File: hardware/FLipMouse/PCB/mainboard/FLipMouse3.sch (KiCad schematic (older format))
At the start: 81 parts, among them J1 SJ2-3574A, J2 SJ2-3574A, J3 M50-3900542, J4 Conn_ARM_JTAG_SWD_10, J5 Conn_02x05_Odd_Even, J6 USB_OTG, J7 Conn_01x06, Q1 BC847, Q2 BC847, Q3 BSH108, Q4 BSH108, Q5 BSH108, SW1 SW_Push, SW2 SW_Push, U1 ESP32-WROOM, U2 TSOP4838, U3 LPC11U14FBD, U4 TSR_1-2433, U5 MPXV7007GP, Y1 JA-12.000-18-DFE

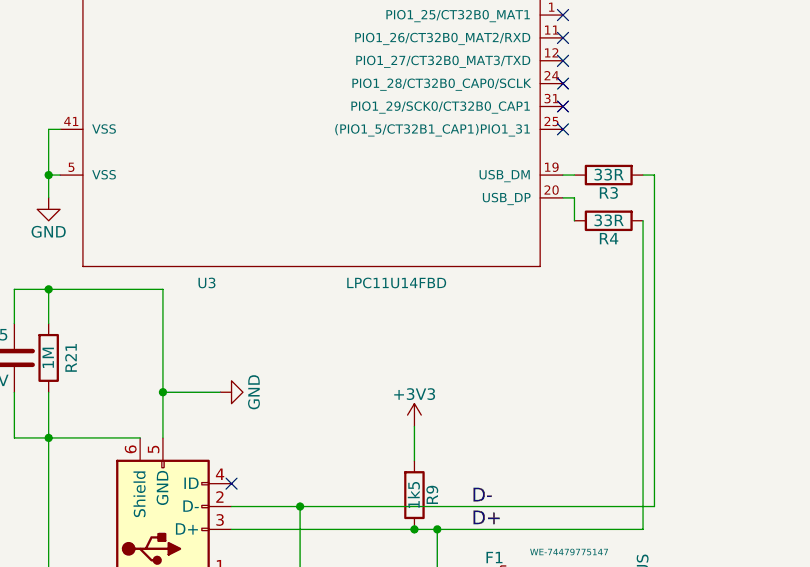
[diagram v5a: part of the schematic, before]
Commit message: Changed USB chipset to LPC11U__2__4 (from LPC11U14): This introduces the possibility to use the USB-MSD bootloader for software updates. Otherwise we would need either a serial adapter, a custom bootloader or a programming software within the ESP32 (and more nets between these two chips).
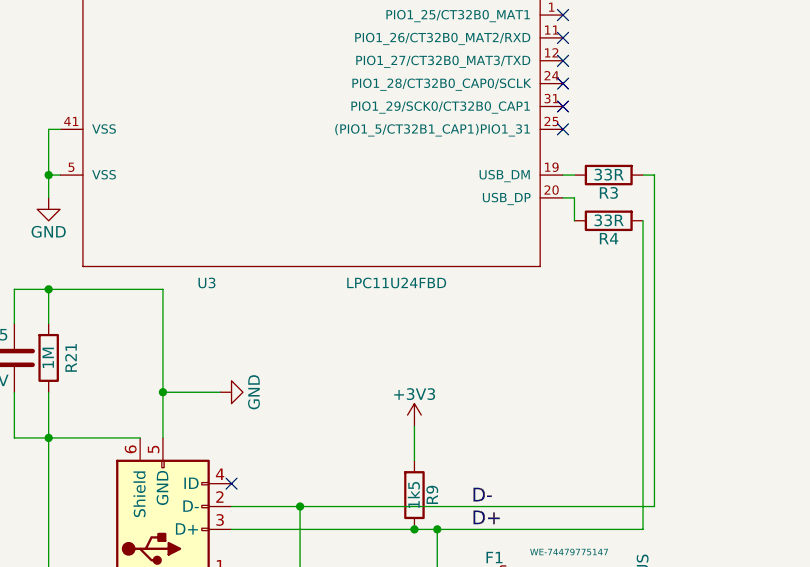
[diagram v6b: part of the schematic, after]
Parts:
- U3: value LPC11U14FBD -> LPC11U24FBD
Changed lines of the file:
@@
 P 2400 3500
 F 0 "U3" H 1900 1000 45  0000 L BNN
-F 1 "LPC11U14FBD" H 2550 1000 45  0000 L BNN
+F 1 "LPC11U24FBD" H 2550 1000 45  0000 L BNN
 F 2 "Package_QFP:LQFP-48_7x7mm_P0.5mm" H 2430 3650 20  0001 C CNN
 F 3 "" H 2400 3500 60  0001 C CNN

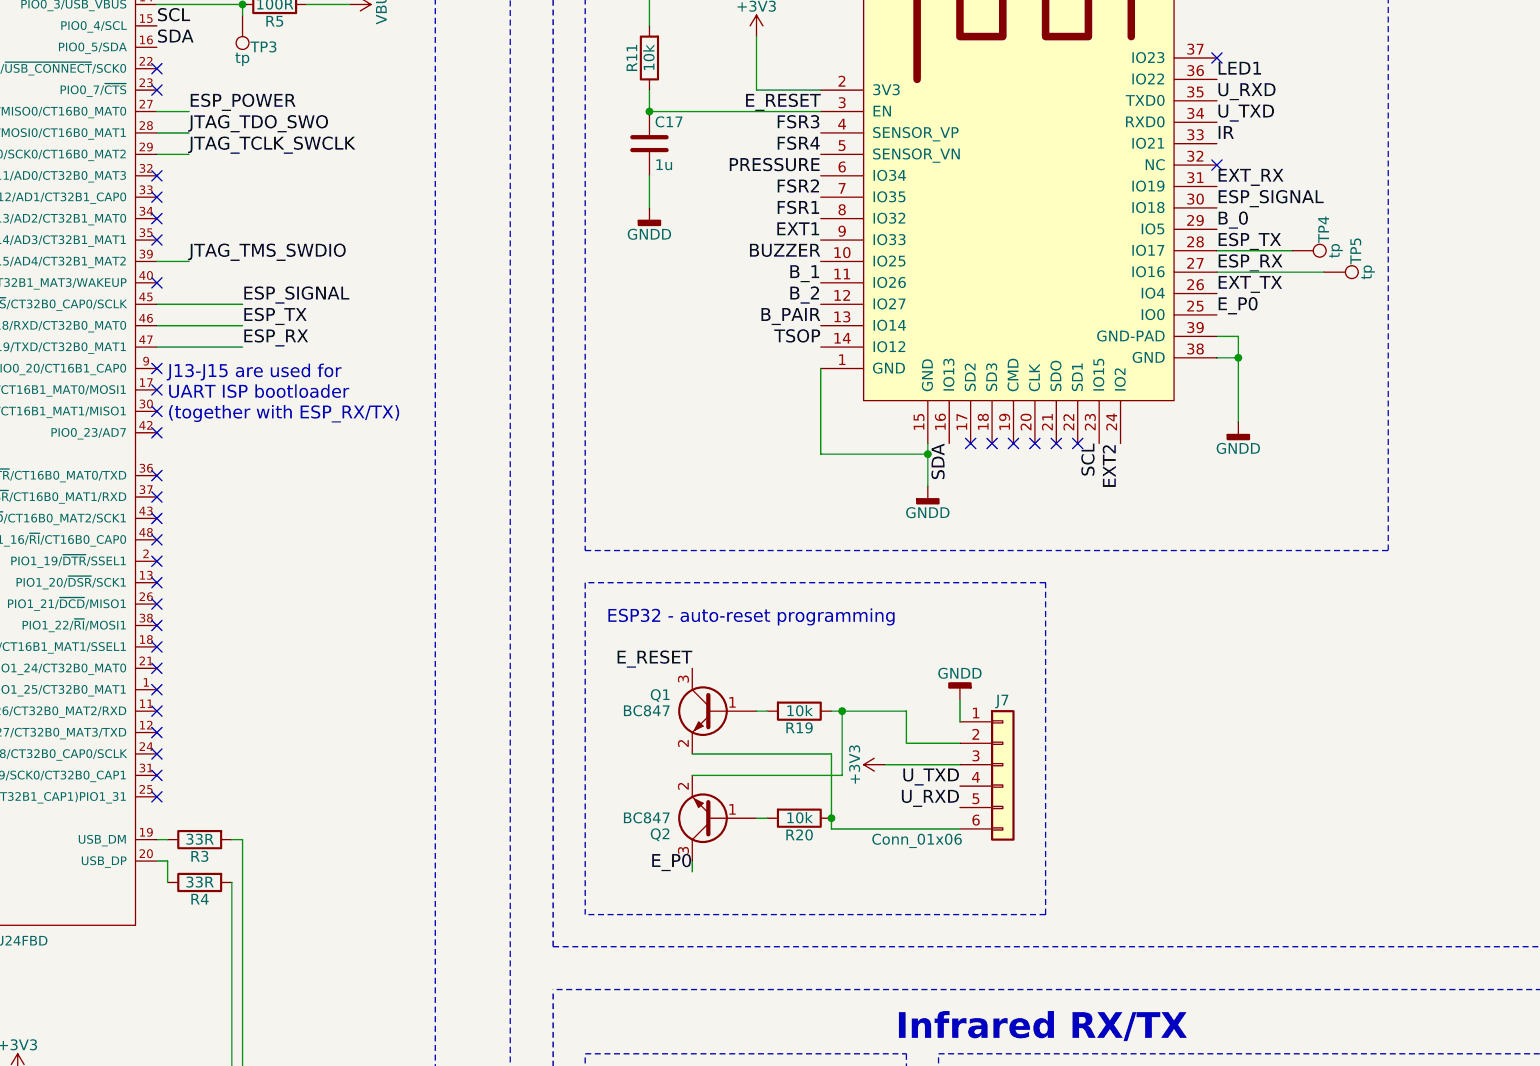
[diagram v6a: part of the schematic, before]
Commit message: Updated FLipMouse PCB: - Routed ADC inputs (FSR+pressure) to LPC11 too (in case of crappy ESP ADC values) - Added ESP32 auto-reset pins to LPC11 (enabling programming via LPC USB) - Cleanup regarding edge to trace spacing
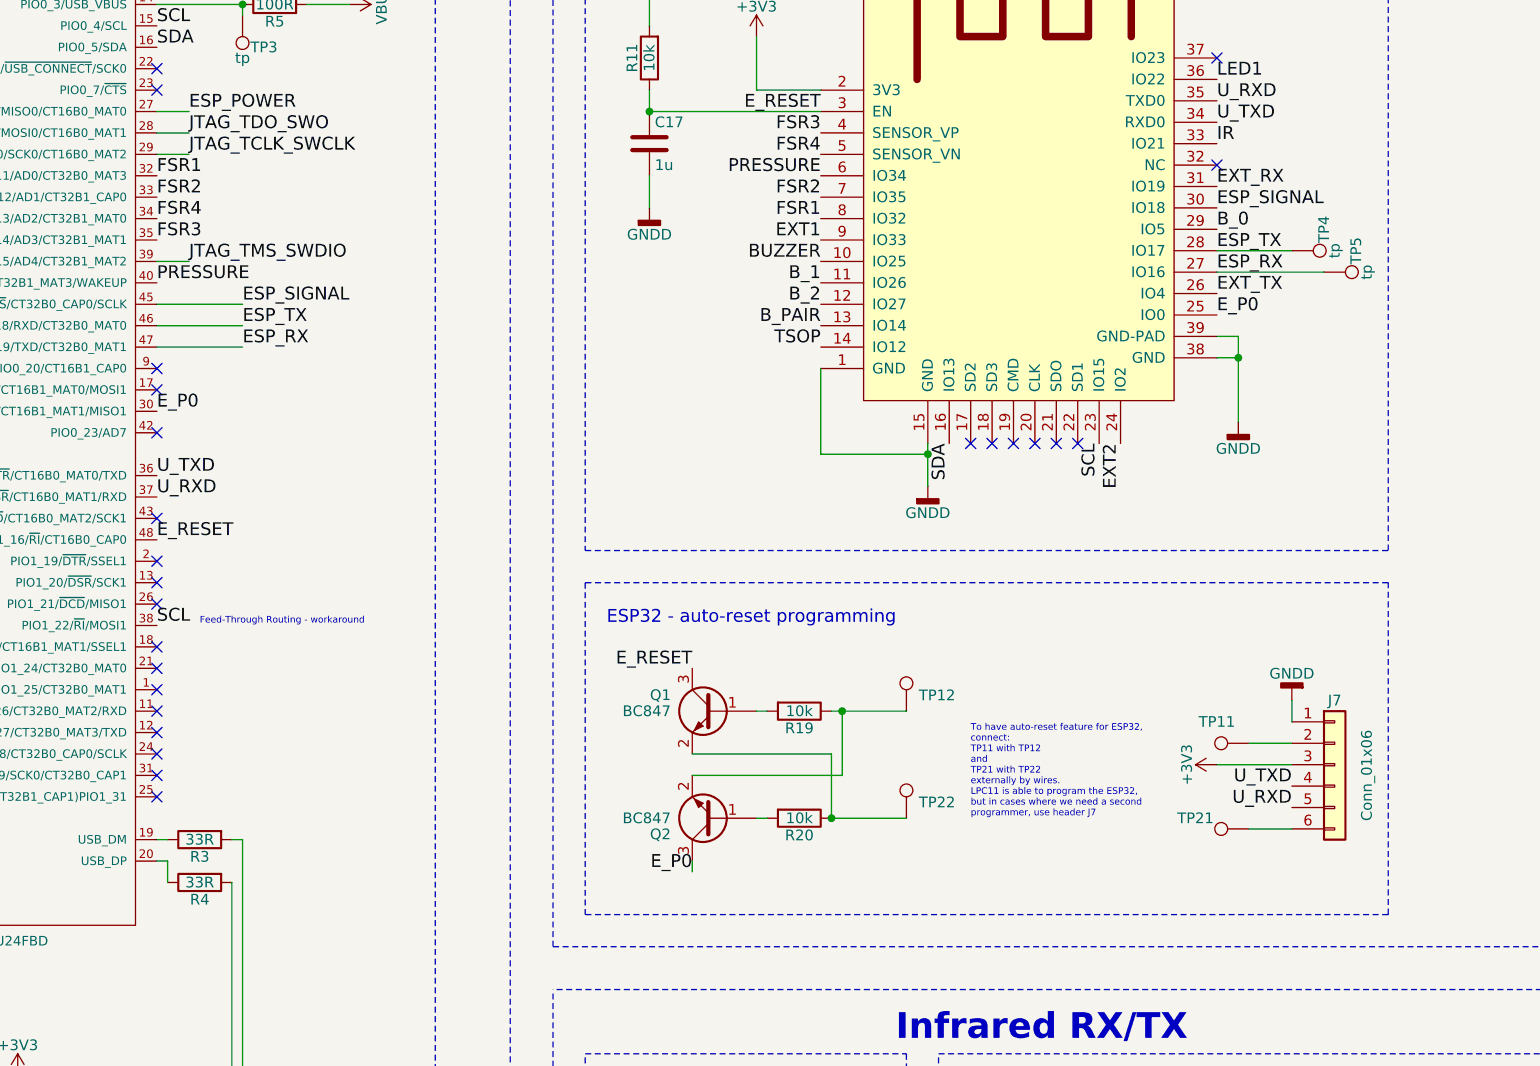
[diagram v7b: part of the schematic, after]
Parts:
- added TP11, TP12, TP21, TP22: TP, TestPoint:TestPoint_Pad_D1.0mm, symbol Connector:TestPoint
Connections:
- net E_P0: now also U3.30 (PIO0_22/AD6/CT16B1_MAT1/MISO1)
- net E_RESET: now also U3.48 (PIO1_16/~RI~/CT16B0_CAP0)
- net FSR1: now also U3.32 (TDI/PIO0_11/AD0/CT32B0_MAT3)
- net FSR2: now also U3.33 (TMS/PIO0_12/AD1/CT32B1_CAP0)
- net FSR3: now also U3.35 (~TRST~/PIO0_14/AD3/CT32B1_MAT1)
- net FSR4: now also U3.34 (TDO/PIO0_13/AD2/CT32B1_MAT0)
- net PRESSURE: now also U3.40 (PIO0_16/AD5/CT32B1_MAT3/WAKEUP)
- net SCL: now also U3.38 (PIO1_22/~RI~/MOSI1)
- net U_RXD: now also U3.37 (PIO1_14/~DSR~/CT16B0_MAT1/RXD)
- net U_TXD: now also U3.36 (PIO1_13/~DTR~/CT16B0_MAT0/TXD)
- net at Q2.2 (E), R19.1: now also TP12.1; no longer J7.2 (Pin_2)
- net at Q1.2 (E), R20.1: now also TP22.1; no longer J7.6 (Pin_6)
- new net: J7.2 (Pin_2), TP11.1
- new net: J7.6 (Pin_6), TP21.1
- no-connect marks 45 -> 35
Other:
- note added: "Feed-Through Routing - workaround"
- note added: "To have auto-reset feature for ESP32,\nconnect:\nTP11 with TP12\nand\nTP21 with TP22\nexternally by wires.\nLPC11 is able to program the ESP32, \nbut in cases where we need a second \nprogrammer, use header J7"
- note removed: "J13-J15 are used for \nUART ISP bootloader\n(together with ESP_RX/TX)"
- moved on the sheet: J7
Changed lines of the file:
@@
 Sheet 1 1
 Title "FLipMouse3"
-Date "2018-11-15"
+Date "2018-12-02"
 Rev "v3.1"
 Comp "AsTeRICS Foundation"
@@
 L Connector_Generic:Conn_01x06 J7
 U 1 1 5A82E80B
-P 7450 5150
-F 0 "J7" H 7450 5450 50  0000 C CNN
-F 1 "Conn_01x06" H 7050 4800 50  0000 C CNN
-F 2 "Connector_PinSocket_1.27mm:PinSocket_1x06_P1.27mm_Vertical" H 7450 5150 50  0001 C CNN
-F 3 "" H 7450 5150 50  0001 C CNN
-	1    7450 5150
+P 9000 5150
+F 0 "J7" H 9000 5450 50  0000 C CNN
+F 1 "Conn_01x06" V 9150 5100 50  0000 C CNN
+F 2 "Connector_PinSocket_1.27mm:PinSocket_1x06_P1.27mm_Vertical" H 9000 5150 50  0001 C CNN
+F 3 "" H 9000 5150 50  0001 C CNN
+	1    9000 5150
 	1    0    0    -1
 $EndComp
@@
 	0    1    1    0
 $EndComp
-Text Label 7250 5350 2    60   ~ 0
+Text Label 8800 5350 2    60   ~ 0
 U_RXD
-Text Label 7250 5250 2    60   ~ 0
+Text Label 8800 5250 2    60   ~ 0
 U_TXD
 $Comp
 L power:GNDD #PWR020
 U 1 1 5A83058B
-P 7250 4850
-F 0 "#PWR020" H 7250 4600 50  0001 C CNN
-F 1 "GNDD" H 7250 4725 50  0000 C CNN
-F 2 "" H 7250 4850 50  0001 C CNN
-F 3 "" H 7250 4850 50  0001 C CNN
-	1    7250 4850
+P 8800 4850
+F 0 "#PWR020" H 8800 4600 50  0001 C CNN
+F 1 "GNDD" H 8800 4725 50  0000 C CNN
+F 2 "" H 8800 4850 50  0001 C CNN
+F 3 "" H 8800 4850 50  0001 C CNN
+	1    8800 4850
 	-1   0    0    1
 $EndComp
@@
 L power:+3V3 #PWR021
 U 1 1 5A83079E
-P 6900 5150
-F 0 "#PWR021" H 6900 5000 50  0001 C CNN
-F 1 "+3V3" H 6900 5290 50  0000 C CNN
-F 2 "" H 6900 5150 50  0001 C CNN
-F 3 "" H 6900 5150 50  0001 C CNN
-	1    6900 5150
+P 8450 5150
+F 0 "#PWR021" H 8450 5000 50  0001 C CNN
+F 1 "+3V3" H 8450 5290 50  0000 C CNN
+F 2 "" H 8450 5150 50  0001 C CNN
+F 3 "" H 8450 5150 50  0001 C CNN
+	1    8450 5150
 	0    -1   -1   0
 $EndComp
@@
 NoConn ~ 3500 1500
 NoConn ~ 3500 2000
-NoConn ~ 3500 4100
-NoConn ~ 3500 2400
-NoConn ~ 3500 2600
-NoConn ~ 3500 2500
-NoConn ~ 3500 2700
-NoConn ~ 3500 2900
+NoConn ~ 3500 5200
 NoConn ~ 3500 3300
 NoConn ~ 3500 3600
-NoConn ~ 3500 3800
 NoConn ~ 3500 4300
 NoConn ~ 3500 4400
-NoConn ~ 3500 4500
 NoConn ~ 3500 4600
 NoConn ~ 3500 4800
 NoConn ~ 3500 5100
-NoConn ~ 3500 5200
 NoConn ~ 3500 5300
 NoConn ~ 8450 2350
@@
 NoConn ~ 3500 5000
 NoConn ~ 3500 4900
-NoConn ~ 3500 3900
 Text Label 7200 3650 3    60   ~ 0
 SDA
@@
 Wire Wire Line
 	6000 5200 6700 5200
-Connection ~ 6650 5400
 Wire Wire Line
 	6000 5100 6650 5100
 Wire Wire Line
-	6650 5450 7250 5450
-Wire Wire Line
 	6650 5100 6650 5400
 Wire Wire Line
@@
 	6650 4900 6700 4900
 Wire Wire Line
-	7000 4900 7000 5050
-Wire Wire Line
-	7000 5050 7250 5050
-Wire Wire Line
-	6900 5150 7250 5150
-Wire Wire Line
-	7250 4950 7250 4850
+	8450 5150 8800 5150
+Wire Wire Line
+	8800 4950 8800 4850
 Connection ~ 15100 5500
 Wire Wire Line
@@
 	14750 2250 14750 900
 Wire Notes Line
-	7650 5850 7650 4300
-Wire Notes Line
-	7650 4300 5500 4300
+	9250 5850 9250 4300
+Wire Notes Line
+	9250 4300 5500 4300
 Wire Notes Line
 	5500 4300 5500 5850
@@
 Wire Wire Line
 	6700 4900 7000 4900
-Wire Wire Line
-	6650 5400 6650 5450
 Wire Wire Line
 	15100 5500 15350 5500
@@
 SCL
 NoConn ~ 3500 3400
-NoConn ~ 3500 3500
 NoConn ~ 3500 4000
 NoConn ~ 3500 4200
@@
 Wire Wire Line
 	3500 1600 3900 1600
-Text Notes 3550 3550 0    60   ~ 0
-J13-J15 are used for \nUART ISP bootloader\n(together with ESP_RX/TX)
 Text Notes 12350 800  0    120  ~ 24
 User Input / Output
@@
 Extension header
 Wire Notes Line
-	7650 5850 5500 5850
+	9250 5850 5500 5850
 Text Notes 6550 800  0    120  ~ 24
 ESP32 - main processor
@@
 	11500 1700 11500 2300
 NoConn ~ 11400 2000
+Text Label 3500 2400 0    60   ~ 0
+FSR1
+Text Label 3500 2500 0    60   ~ 0
+FSR2
+Text Label 3500 2700 0    60   ~ 0
+FSR3
+Text Label 3500 2600 0    60   ~ 0
+FSR4
+Text Label 3500 2900 0    60   ~ 0
+PRESSURE
+Text Label 3500 3500 0    60   ~ 0
+E_P0
+Text Label 3500 3800 0    60   ~ 0
+U_TXD
+Text Label 3500 3900 0    60   ~ 0
+U_RXD
+Text Label 3500 4100 0    60   ~ 0
+E_RESET
+$Comp
+L Connector:TestPoint TP11
+U 1 1 5C06E7F7
+P 8600 5050
+F 0 "TP11" V 8700 5200 50  0000 C CNN
+F 1 "TP" V 8704 5124 50  0001 C CNN
+F 2 "TestPoint:TestPoint_Pad_D1.0mm" H 8800 5050 50  0001 C CNN
+F 3 "~" H 8800 5050 50  0001 C CNN
+	1    8600 5050
+	0    -1   -1   0
+$EndComp
+$Comp
+L Connector:TestPoint TP21
+U 1 1 5C06E8C9
+P 8600 5450
+F 0 "TP21" V 8650 5700 50  0000 C CNN
+F 1 "TP" V 8700 5650 50  0001 C CNN
+F 2 "TestPoint:TestPoint_Pad_D1.0mm" H 8800 5450 50  0001 C CNN
+F 3 "~" H 8800 5450 50  0001 C CNN
+	1    8600 5450
+	0    -1   -1   0
+$EndComp
+$Comp
+L Connector:TestPoint TP12
+U 1 1 5C06E995
+P 7000 4900
+F 0 "TP12" H 7058 4974 50  0000 L CNN
+F 1 "TP" H 7058 4929 50  0001 L CNN
+F 2 "TestPoint:TestPoint_Pad_D1.0mm" H 7200 4900 50  0001 C CNN
+F 3 "~" H 7200 4900 50  0001 C CNN
+	1    7000 4900
+	1    0    0    -1
+$EndComp
+$Comp
+L Connector:TestPoint TP22
+U 1 1 5C06EA65
+P 7000 5400
+F 0 "TP22" H 7058 5474 50  0000 L CNN
+F 1 "TP" H 7058 5429 50  0001 L CNN
+F 2 "TestPoint:TestPoint_Pad_D1.0mm" H 7200 5400 50  0001 C CNN
+F 3 "~" H 7200 5400 50  0001 C CNN
+	1    7000 5400
+	1    0    0    -1
+$EndComp
+Wire Wire Line
+	6650 5400 7000 5400
+Connection ~ 6650 5400
+Wire Wire Line
+	8600 5050 8800 5050
+Wire Wire Line
+	8600 5450 8800 5450
+Text Notes 7300 5400 0    31   ~ 0
+To have auto-reset feature for ESP32,\nconnect:\nTP11 with TP12\nand\nTP21 with TP22\nexternally by wires.\nLPC11 is able to program the ESP32, \nbut in cases where we need a second \nprogrammer, use header J7
+Text Label 3500 4500 0    60   ~ 0
+SCL
+Text Notes 3700 4500 0    31   ~ 0
+Feed-Through Routing - workaround
 $EndSCHEMATC

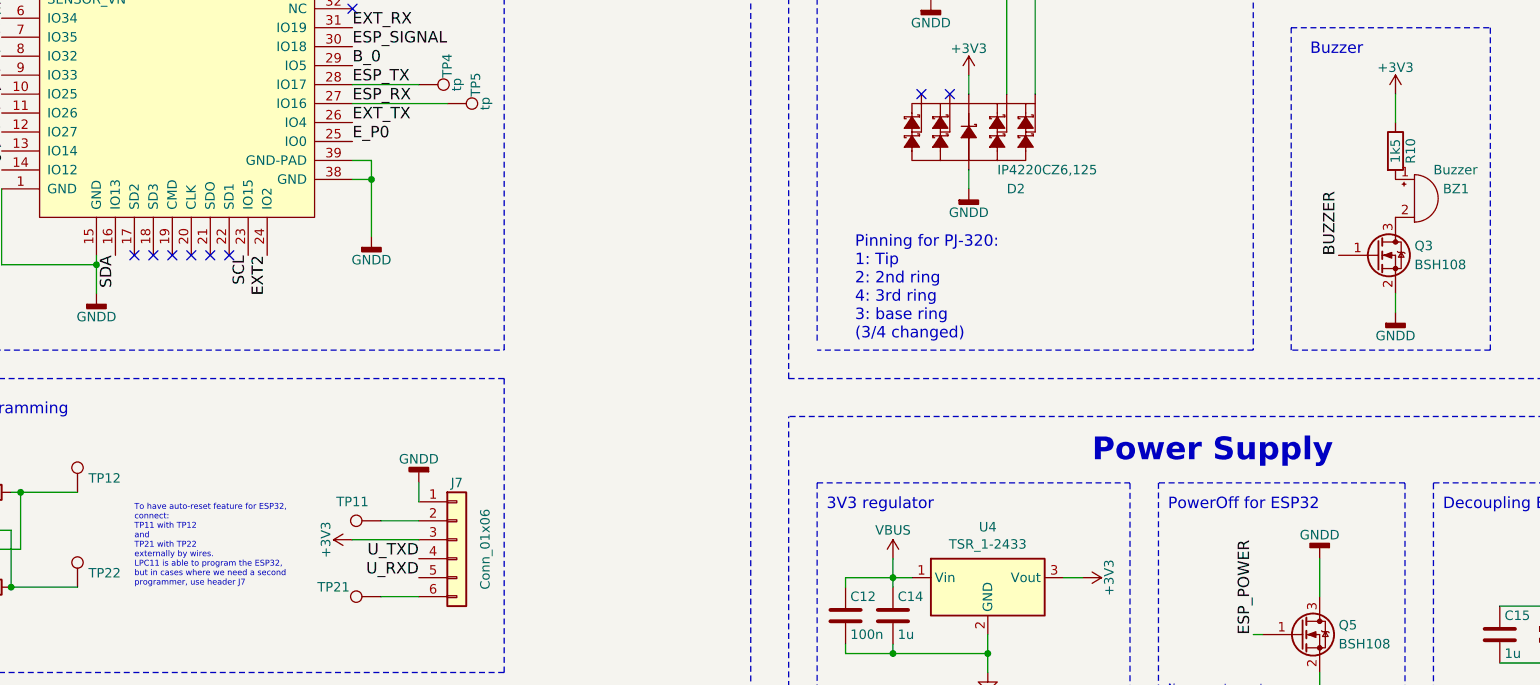
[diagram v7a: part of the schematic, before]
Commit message: Small documentation updates. Fixed R10, according to batch documentation (batch 'a'), from 1k5 to 15R (series resistor for buzzer)
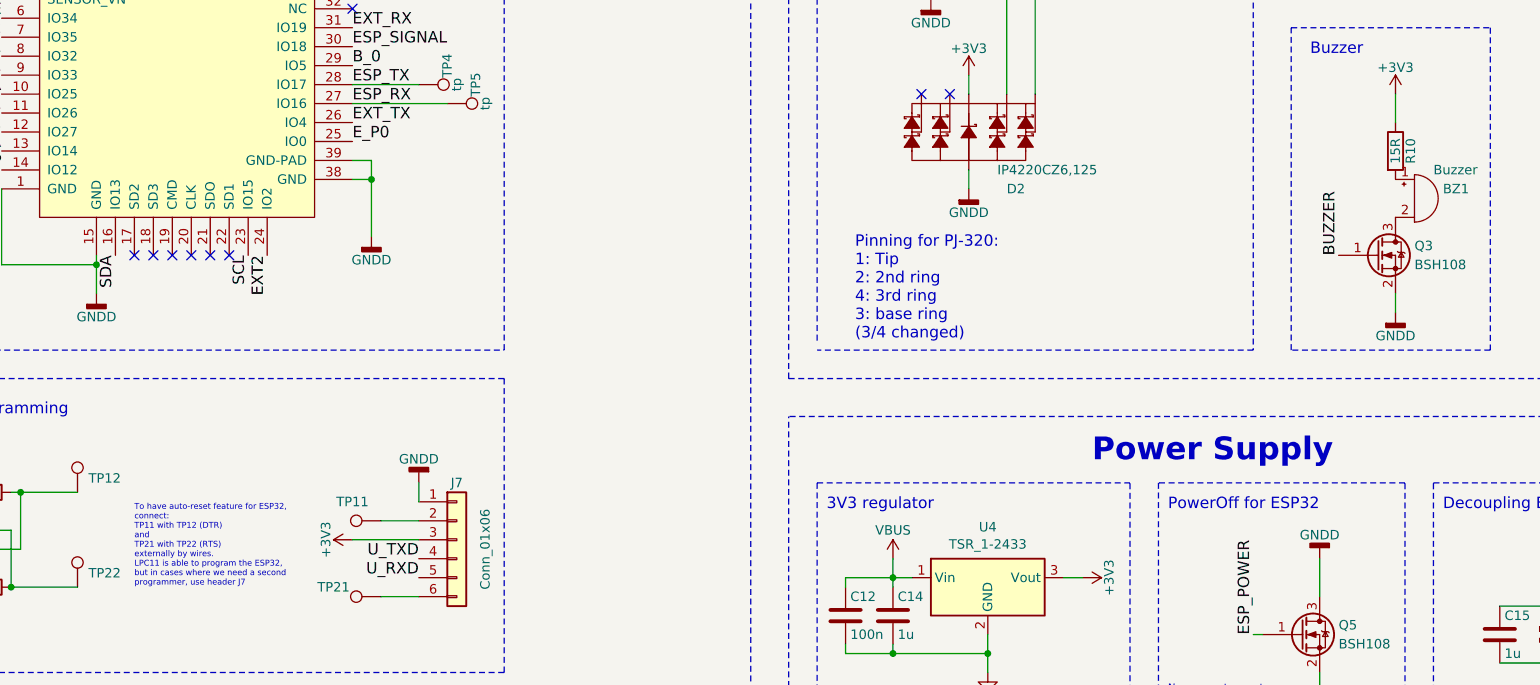
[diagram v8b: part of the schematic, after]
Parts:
- R10: value 1k5 -> 15R
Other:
- note added: "To have auto-reset feature for ESP32,\nconnect:\nTP11 with TP12 (DTR)\nand\nTP21 with TP22 (RTS)\nexternally by wires.\nLPC11 is able to program the ESP32, \nbut in cases where we need a second \nprogrammer, use header J7"
- note removed: "To have auto-reset feature for ESP32,\nconnect:\nTP11 with TP12\nand\nTP21 with TP22\nexternally by wires.\nLPC11 is able to program the ESP32, \nbut in cases where we need a second \nprogrammer, use header J7"
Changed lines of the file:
@@
 P 13950 3100
 F 0 "R10" V 14030 3100 50  0000 C CNN
-F 1 "1k5" V 13950 3100 50  0000 C CNN
+F 1 "15R" V 13950 3100 50  0000 C CNN
 F 2 "Resistor_SMD:R_0603_1608Metric" V 13880 3100 50  0001 C CNN
 F 3 "" H 13950 3100 50  0001 C CNN
@@
 	8600 5450 8800 5450
 Text Notes 7300 5400 0    31   ~ 0
-To have auto-reset feature for ESP32,\nconnect:\nTP11 with TP12\nand\nTP21 with TP22\nexternally by wires.\nLPC11 is able to program the ESP32, \nbut in cases where we need a second \nprogrammer, use header J7
+To have auto-reset feature for ESP32,\nconnect:\nTP11 with TP12 (DTR)\nand\nTP21 with TP22 (RTS)\nexternally by wires.\nLPC11 is able to program the ESP32, \nbut in cases where we need a second \nprogrammer, use header J7
 Text Label 3500 4500 0    60   ~ 0
 SCL
